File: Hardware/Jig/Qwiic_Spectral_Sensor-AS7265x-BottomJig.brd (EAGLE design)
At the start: 35.6 x 40.6 mm, 93 parts, among them J2 Serial Interface, J5 Flash Programming, J8 PTH, U1 AS72651, U3 4MB Flash, U5 AS72653, U6 AS72652

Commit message: Silk changes before panelization
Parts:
- removed C1: 1.0uF, SparkFun-Capacitors:0603
- removed C2, C4, C6: 0.1uF, SparkFun-Capacitors:0603
- removed C3, C5, C7: 10uF, SparkFun-Capacitors:0603
- removed D1: BLUE, SparkFun-LED:LED-0603
- removed D2: 5700k, SparkFun-LED:SUPER_BRIGHT_SMD_LED_3014
- removed D3: IR, SparkFun-LED:LED-0603
- removed D4: RED, SparkFun-LED:LED-0603
- removed D5: UV, SparkFun-LED:PLCC-2
- removed FD1, FD2, FD3, FD4: FIDUCIAL1X2, SparkFun-Aesthetics:FIDUCIAL-1X2
- removed J1, J4: (no value), SparkFun-Connectors:1X04_1MM_RA
- removed JP1: (no value), SparkFun-Jumpers:SMT-JUMPER_3_2-NC_TRACE_SILK
- removed JP2: (no value), SparkFun-Jumpers:SMT-JUMPER_2_NO_SILK
- removed JP3, JP4, JP5: (no value), SparkFun-Jumpers:SMT-JUMPER_2_NC_TRACE_NO-SILK
- removed R10, R11, R12, R9: 2.2k, SparkFun-Resistors:0603
- removed R7, R8: 10k, SparkFun-Resistors:0603
- removed TP1: (no value), SparkFun-Connectors:PAD.03X.03
- removed U5: AS72653, Qwiic_Spectral_Sensor-AS7265x:LGA20
- removed U6: AS72652, Qwiic_Spectral_Sensor-AS7265x:LGA20
- added BUTTON1, BUTTON2: CAPSENSE_BUTTON_PAD_ONLY, Testing:CAPSENSE_BUTTON_PADS_ONLY
- added FRAME2: FRAME-LEDGER, SparkFun-Aesthetics:CREATIVE_COMMONS
- added H5, H6: STAND-OFF, SparkFun-Hardware:STAND-OFF
- added J_SCL, J_SCL3, J_SDA, J_SDA1: JUMPER-SMT_2_NO_NO-SILK, SparkFun-Jumpers:SMT-JUMPER_2_NO_NO-SILK
- added J_SCL1, J_SCL2, J_SCL4, J_SCL5: (no value), SparkFun-Jumpers:SMT-JUMPER_2_NO_NO-SILK
- added MT_FAIL, MT_PASS, PROGRAM, PT_FAIL, PT_PASS, S0, S1, S2, S3, S4: (no value), Testing:LED-1206
- added R6: 330, SparkFun-Resistors:0603
- added U2: 74LVC4066, Testing:SO14
- R1, R3, R4, R5: value 10k -> 330
- R2: value 1k -> 330
- U$1, U$36, U$37: device buzzard_labels (7):#0 -> SparkFun-Hardware:STAND-OFF-TIGHT
- U$38: device buzzard_labels (7):#1 -> SparkFun-Hardware:STAND-OFF-TIGHT
- U$39, U$40: device buzzard_labels (7):#1 -> SparkFun-Hardware:NUBBIN_LOCKER
- U1: value AS72651 -> FLYING_JALAPENO; device Qwiic_Spectral_Sensor-AS7265x:LGA20 -> Testing:FLYING_JALAPENO_V3_M
- U3: value 4MB Flash -> 74LVC4066; device SparkFun-IC-Memory:SO08 -> Testing:SO14
- moved H2 120.9 mm to (123.2, 2.54)
- moved H4 117.4 mm to (123.2, 106.7)
- moved U$38 108.9 mm to (84.5, 91.4), flipped to the top
- moved U3 106.2 mm to (111.8, 83.8), turned to 90 degrees
- moved U1 95.0 mm to (64.8, 109.2), turned to 0 degrees
- moved R1 83.2 mm to (105.4, 16.5), turned to 0 degrees
- moved U$40 78.1 mm to (63.5, 94.7), flipped to the top, turned to 0 degrees
- moved U$37 76.6 mm to (84.5, 50.8), flipped to the top
- moved U$36 74.8 mm to (42.5, 91.4), flipped to the top, turned to 0 degrees
- moved U$6 70.6 mm to (70.6, 77.5), turned to 240 degrees
- moved U$10 70.3 mm to (70.5, 82.5)
- moved BULB2 68.3 mm to (73.9, 75.8)
- moved BULB3 68.3 mm to (63.5, 57.8)
- moved H3 68.3 mm to (53.3, 53.3)
- moved J5 68.3 mm to (63.5, 85.1)
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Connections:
- removed net !RST-ADDR: U1.13, U6.2
- removed net I2C_ENB: JP2.2, R3.1, TP1.P$1, U1.8
- removed net N$1: D4.C, R2.2
- removed net N$11: D5.A, JP3.1
- removed net N$12: R8.2, U5.7
- removed net N$13: R7.2, U5.5
- removed net N$2: D1.C, U1.18
- removed net N$3: R5.2, U6.7
- removed net N$4: JP1.3, R12.2
- removed net N$5: JP1.1, R11.2
- removed net N$6: D2.A, JP4.1
- removed net N$8: D3.A, JP5.1
- removed net N$9: R1.2, U6.5
- removed net SCL_S: R9.1, U1.20, U5.9, U6.9
- removed net SDA_S: R10.1, U1.1, U5.10, U6.10
- new net 3.3V_POWER: U1.2, U1.32, U2.14, U3.14
- new net 5V_POWER: U1.3, U1.33
- new net JALAPENO_CS: J_SDA1.1, U1.60, U3.11
- new net JALAPENO_I2C_EN: U1.24, U2.13, U2.5
- new net JALAPENO_MISO: J_SCL5.1, U1.29, U3.1
- new net JALAPENO_MOSI: J_SCL3.1, U1.59, U3.4
- new net JALAPENO_RX1-I: J_SDA.1, U1.52, U2.11
- new net JALAPENO_SCK: J_SCL4.1, U1.30, U3.8
- new net JALAPENO_SCL: J_SCL.1, U1.53, U2.4
- new net JALAPENO_SDA: J_SCL2.1, U1.23, U2.1
- new net JALAPENO_SERIAL_EN: U1.54, U2.12, U2.6
- new net JALAPENO_SPI_EN: U3.12, U3.13, U3.5, U3.6
- new net JALAPENO_TX1-O: J_SCL1.1, U1.22, U2.8
- new net J_24: U1.25
- new net J_25: U1.55
- new net J_26: U1.26
- new net J_27: U1.56
- new net J_28: U1.27
- new net J_29: U1.57
- new net J_30: U1.28
- new net J_A0: U1.37
- new net J_A1: U1.8
- new net J_A2: U1.38
- new net J_A3: U1.9
- new net J_A4: U1.39
- new net J_PWM2: U1.14
- new net J_PWM3: U1.44
- new net J_PWM4: U1.15
- new net J_PWM5: U1.45
- new net N$10: PT_FAIL.A, U1.36
- new net N$14: MT_PASS.A, U1.6
- new net N$15: MT_FAIL.A, U1.35
- new net N$16: BUTTON2.CAPSENSE_PAD, U1.58
- new net N$17: BUTTON1.CAPSENSE_PAD, U1.5
- new net N$18: R1.2, U1.19
- new net N$19: PROGRAM.A, R1.1
- new net N$20: R6.2, U1.46
- new net N$21: R5.2, U1.17
- new net N$22: R4.2, U1.47
- new net N$23: R3.2, U1.18
- new net N$24: R2.2, U1.48
- new net N$25: R6.1, S4.A
- new net N$26: R5.1, S3.A
- new net N$27: R4.1, S2.A
- new net N$28: R3.1, S1.A
- new net N$29: R2.1, S0.A
- new net N$7: PT_PASS.A, U1.7
- new net TARGET_CS: J_SDA1.2, U3.10
- new net TARGET_MISO: J_SCL5.2, U3.2
- new net TARGET_MOSI: J_SCL3.2, U3.3
- new net TARGET_RX: J_SCL1.2, U2.9
- new net TARGET_SCK: J_SCL4.2, U3.9
- new net TARGET_SCL: J_SCL.2, U2.3
- new net TARGET_SDA: J_SCL2.2, U2.2
- new net TARGET_TX: J_SDA.2, U2.10
- net !CS_EE: no longer U1.6, U3.1
- net !INT: no longer U1.9
- net !RST: no longer R4.1, U1.2, U5.2
- net 3.3V: no longer C1.1, C2.1, C3.1, C4.1, C5.1, C6.1, C7.1, D1.A, D4.A, J1.2, J4.2, JP1.2, JP3.2, JP4.2, JP5.2, R10.2, R3.2, R4.2, R9.2, U1.14, U1.17, U3.3, U3.7, U3.8, U5.14, U5.17, U6.14, U6.17
- net GND: now also MT_FAIL.C, MT_PASS.C, PROGRAM.C, PT_FAIL.C, PT_PASS.C, S0.C, S1.C, S2.C, S3.C, S4.C, U1.1, U1.31, U2.7, U3.7; no longer C1.2, C2.2, C3.2, C4.2, C5.2, C6.2, C7.2, J1.1, J4.1, JP2.1, R1.1, R2.1, R5.1, R7.1, R8.1, U1.16, U3.4, U5.16, U6.16
- net LED_DRV: no longer D2.C, U1.15
- net LED_DRV1: no longer D3.C, U6.15
- net LED_DRV2: no longer D5.C, U5.15
- net MISO: no longer U1.5, U3.2
- net MOSI: no longer U1.4, U3.5
- net RX/SCL: no longer J1.4, J4.4, R11.1, U1.11
- net SCK: no longer U1.3, U3.6
- net TX/SDA: no longer J1.3, J4.3, R12.1, U1.12
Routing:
- net 3.3V: track 143.3 -> 0.00 mm, vias 4 -> 0
- net RX/SCL: track 99.0 -> 0.00 mm, vias 6 -> 0
- net TX/SDA: track 93.2 -> 0.00 mm, vias 5 -> 0
- net SDA_S: track 56.9 -> 0.00 mm, vias 3 -> 0
- net SCL_S: track 56.2 -> 0.00 mm, vias 3 -> 0
- net !RST: track 50.8 -> 0.00 mm, vias 3 -> 0
- net !INT: track 30.2 -> 0.00 mm, vias 1 -> 0
- net LED_DRV: track 21.0 -> 0.00 mm, vias 1 -> 0
- net !CS_EE: track 17.6 -> 0.00 mm, vias 2 -> 0
- net I2C_ENB: track 16.8 -> 0.00 mm, vias 1 -> 0
- net MISO: track 15.5 -> 0.00 mm, vias 1 -> 0
- net !RST-ADDR: track 14.9 -> 0.00 mm, vias 2 -> 0
- net N$2: track 11.8 -> 0.00 mm, vias 2 -> 0
- net MOSI: track 9.65 -> 0.00 mm
- net LED_DRV1: track 9.51 -> 0.00 mm
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- removed copper zone on layer 1, net GND
- removed copper zone on layer 16, net GND
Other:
- board size 35.6 x 40.6 mm -> 125.7 x 109.2 mm
- board text added: "#6"
- board text added: "0"
- board text added: "1"
- board text added: "2"
- board text added: "3"
- board text added: "4"
- board text added: "Board Power and Pretest"
- board text added: "DEV-Me"
- board text added: "FAIL"
- board text added: "GPS-Test"
- board text added: "MAIN TEST"
- board text added: "PASS"
- board text added: "PRETEST"
- board text added: "READY TO PROGRAM"
- board text added: "Tap to TEST"
- board text added: "v10"
- board text removed: "V10"

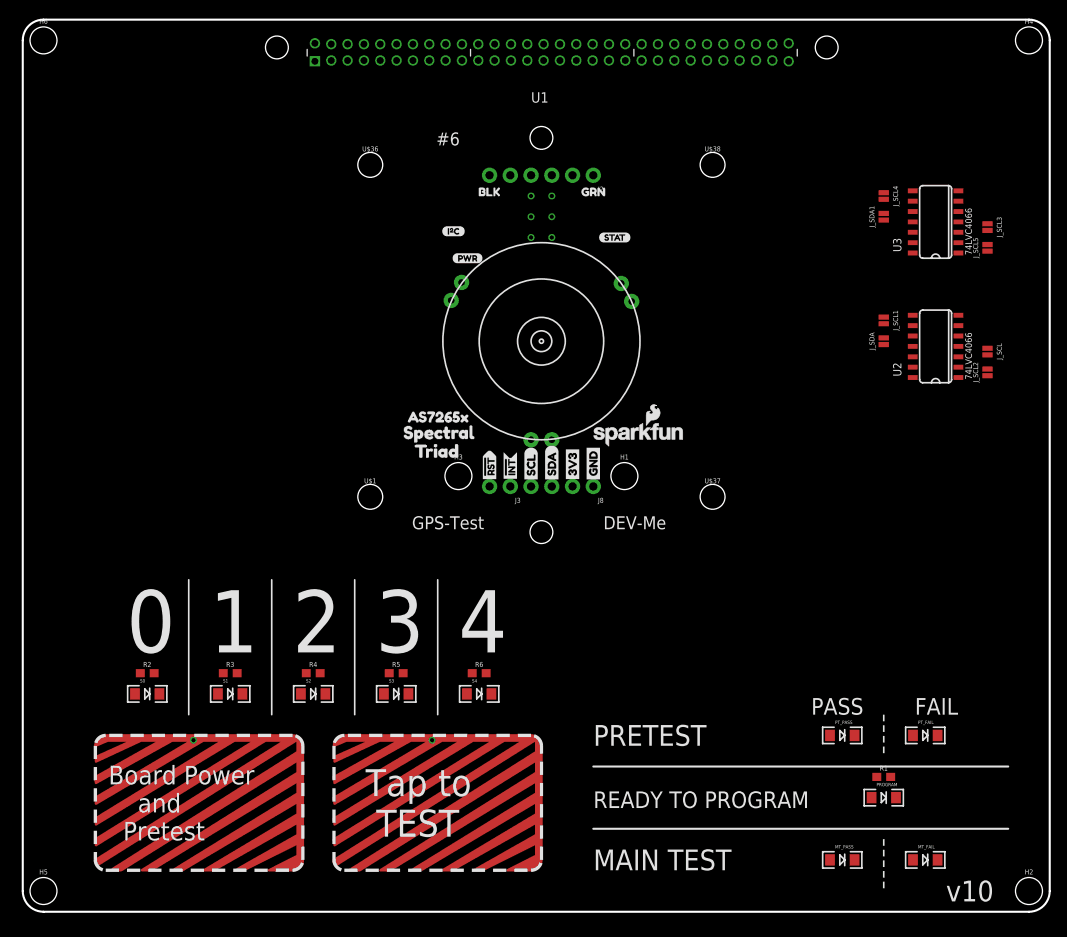
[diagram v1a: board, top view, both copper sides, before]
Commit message: Intermediate committ. Probably ignore the jig files.
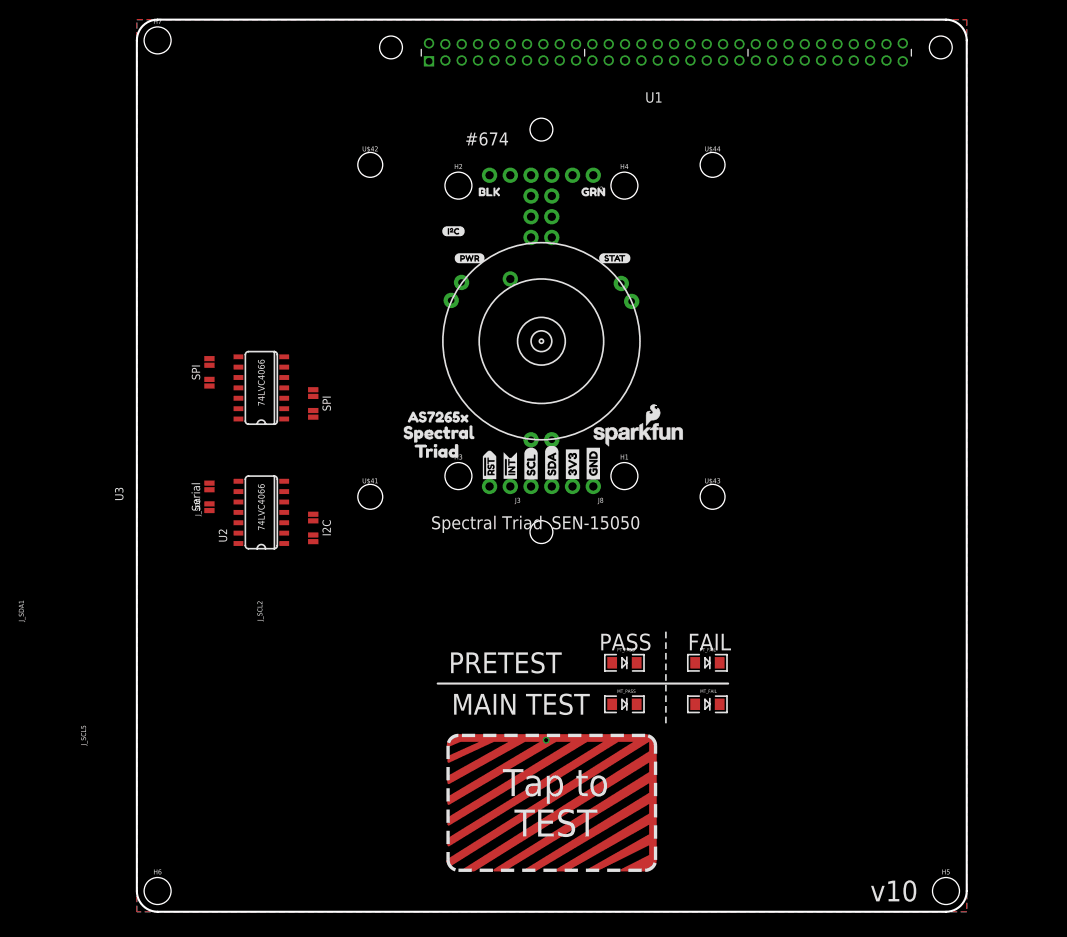
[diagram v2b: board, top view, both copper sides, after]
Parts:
- removed BUTTON1: CAPSENSE_BUTTON_PAD_ONLY, Testing:CAPSENSE_BUTTON_PADS_ONLY
- removed PROGRAM, S0, S1, S2, S3, S4: (no value), Testing:LED-1206
- removed R1, R2, R3, R4, R5, R6: 330, SparkFun-Resistors:0603
- added H7: STAND-OFF, SparkFun-Hardware:STAND-OFF
- added TP1: TEST-POINTPOGO_PTH, SparkFun-Connectors:1X01_NO_SILK
- added U$41, U$42, U$43, U$44: (no value), SparkFun-Hardware:STAND-OFF-TIGHT
- added U$45, U$46: (no value), SparkFun-Hardware:NUBBIN_LOCKER
- J5: device SparkFun-Connectors:2X3_TEST_POINTS -> SparkFun-Connectors:2X3-NS
- U$1, U$36, U$37: device SparkFun-Hardware:STAND-OFF-TIGHT -> buzzard_labels (7):#0
- U$38: device SparkFun-Hardware:STAND-OFF-TIGHT -> buzzard_labels (7):#1
- U$39, U$40: device SparkFun-Hardware:NUBBIN_LOCKER -> buzzard_labels (7):#1
- moved H2 111.1 mm to (53.3, 88.9)
- moved H5 110.5 mm to (113.0, 2.54)
- moved H6 105.1 mm to (16.5, 2.54)
- moved U2 85.0 mm to (29.2, 48.3)
- moved U3 85.0 mm to (29.2, 63.5)
- moved J_SCL 85.0 mm to (35.6, 48.3)
- moved J_SCL1 85.0 mm to (22.9, 52.1)
- moved J_SCL2 85.0 mm to (35.6, 45.7)
- moved J_SCL3 85.0 mm to (35.6, 63.5)
- moved J_SCL4 85.0 mm to (22.9, 67.3)
- moved J_SCL5 85.0 mm to (35.6, 61.0)
- moved J_SDA 85.0 mm to (22.9, 49.5)
- moved J_SDA1 85.0 mm to (22.9, 64.8)
- moved H4 52.6 mm to (73.7, 88.9)
- moved U$1 42.0 mm to (75.6, 76.7), flipped to the bottom, turned to 60 degrees
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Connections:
- net N$16 renamed BUTTON2
- removed net N$17: BUTTON1.CAPSENSE_PAD, U1.5
- removed net N$18: R1.2, U1.19
- removed net N$19: PROGRAM.A, R1.1
- removed net N$20: R6.2, U1.46
- removed net N$21: R5.2, U1.17
- removed net N$22: R4.2, U1.47
- removed net N$23: R3.2, U1.18
- removed net N$24: R2.2, U1.48
- removed net N$25: R6.1, S4.A
- removed net N$26: R5.1, S3.A
- removed net N$27: R4.1, S2.A
- removed net N$28: R3.1, S1.A
- removed net N$29: R2.1, S0.A
- new net I2C_ENB: TP1.1
- net GND: no longer PROGRAM.C, S0.C, S1.C, S2.C, S3.C, S4.C
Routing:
- added copper zone on layer 1, net GND
- added copper zone on layer 16, net GND
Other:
- board size 125.7 x 109.2 mm -> 101.6 x 109.2 mm
- board text added: "#674"
- board text added: "I2C"
- board text added: "SEN-15050"
- board text added: "SPI"
- board text added: "Serial"
- board text added: "Spectral Triad"
- board text removed: "#6"
- board text removed: "0"
- board text removed: "1"
- board text removed: "2"
- board text removed: "3"
- board text removed: "4"
- board text removed: "Board Power and Pretest"
- board text removed: "DEV-Me"
- board text removed: "GPS-Test"
- board text removed: "READY TO PROGRAM"
